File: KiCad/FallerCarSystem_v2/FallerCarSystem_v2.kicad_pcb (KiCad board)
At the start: 2 copper layers, 10 x 10 mm, 76 parts, among them J1 Conn_01x01_Male, J10 Conn_01x01_Male, J11 Conn_01x01_Male, J12 Conn_01x01_Male, J13 Conn_01x01_Male, J14 Conn_01x01_Male, J15 Conn_01x01_Male, J16 Conn_01x01_Male, J17 Conn_01x01_Male, J18 Conn_01x01_Male, J19 Conn_01x01_Male, J2 Conn_01x01_Male, J20 Conn_01x01_Male, J21 Conn_01x01_Male, J22 Conn_01x01_Male, J23 Conn_01x01_Male, J24 Conn_01x01_Male, J25 Conn_01x01_Male, J26 Conn_01x01_Male, J27 Conn_01x01_Male, J28 Conn_01x01_Male, J29 Conn_01x01_Male, J3 Conn_01x01_Male, J30 Conn_01x01_Male, J31 Conn_01x01_Male, J32 Conn_01x01_Male, J33 Conn_01x01_Male, J34 Conn_01x01_Male, J35 Conn_01x01_Male, J36 Conn_01x01_Male, J37 Conn_01x01_Male, J38 Conn_01x01_Male, J4 Conn_01x01_Male, J5 Conn_01x01_Male, J6 Conn_01x01_Male, J7 Conn_01x01_Male, J8 Conn_01x01_Male, J9 Conn_01x01_Male, U1 PIC16F15345-I_GZ, U2 MCP73871-2AA, U3 MCP1725-ADJE_MC_DFN-8

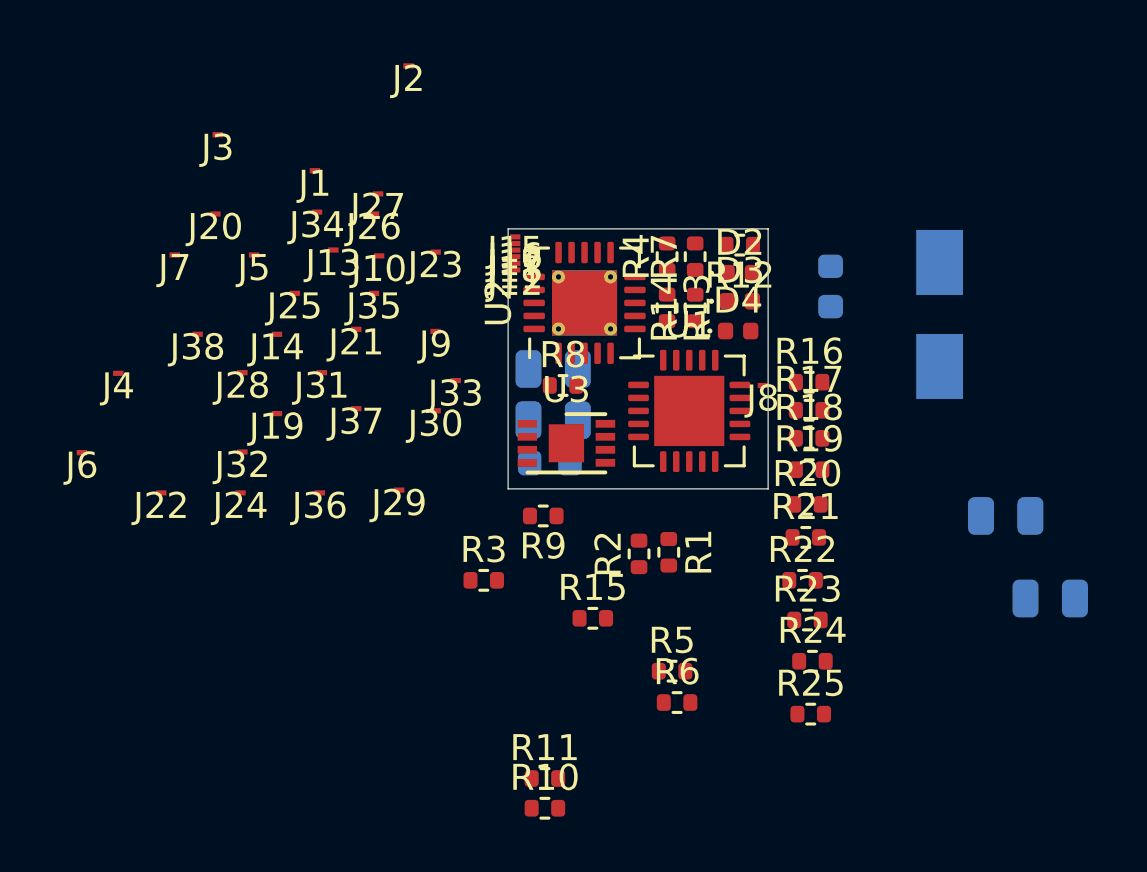
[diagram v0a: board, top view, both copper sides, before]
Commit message: FallerCarSystem_v2 drawing and PCB done. Generated Gerber files.
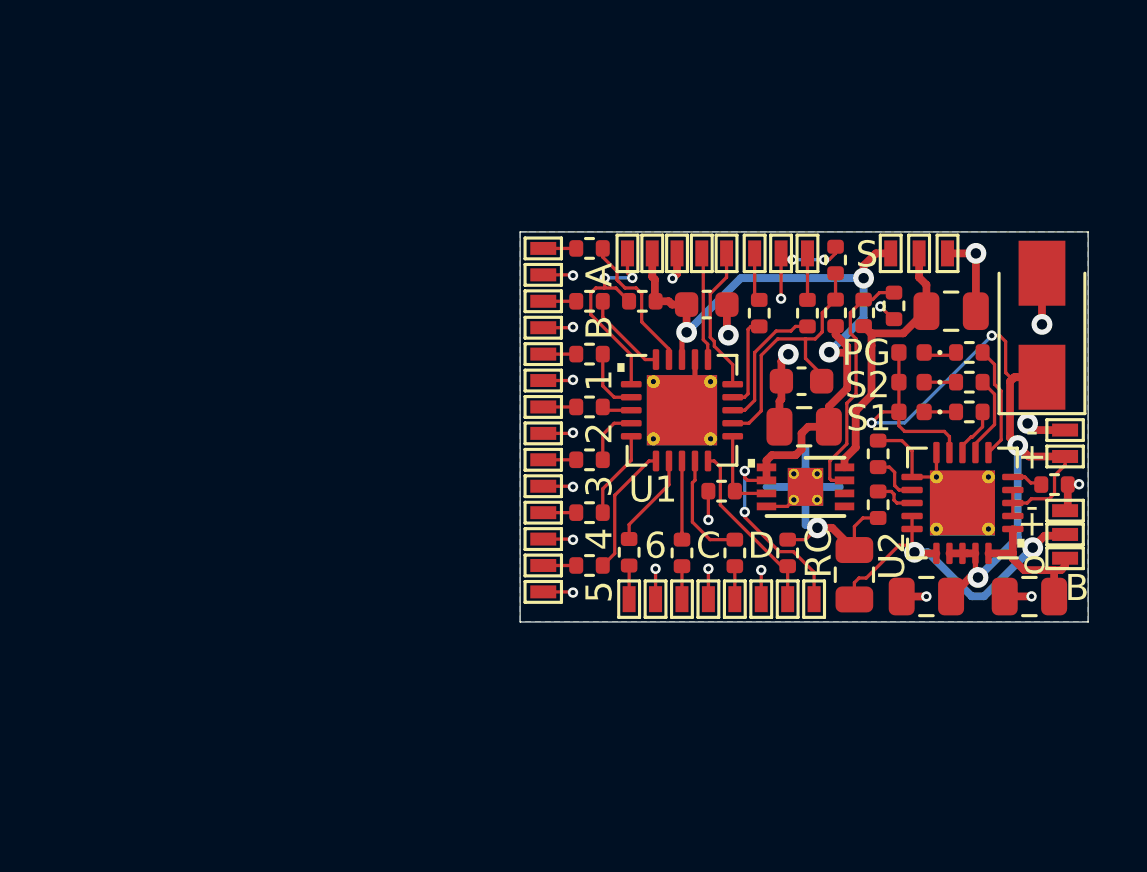
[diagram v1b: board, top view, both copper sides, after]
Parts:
- added C7: 4.7uF, Capacitor_SMD:C_0805_2012Metric, F.Cu at (160.0, 69.1)
- added REF**: ESD-Logo_6.6x6mm_SilkScreen, Symbol:ESD-Logo_6.6x6mm_SilkScreen, B.Cu at (156.7, 64.9)
- C1, C2, C3, C4, C5, C6, D1: moved to F.Cu
- J1, J10, J11, J12, J13, J14, J15, J16, J17, J18, J19, J2, J20, J21, J22, J23, J24, J25, J26, J27, J28, J29, J3, J30, J31, J32, J33, J34, J35, J36, J37, J38, J4, J5, J6, J7, J8, J9: footprint Connector:Finger -> TestPoint:TestPoint_Pad_0.5x1.0mm
- R10: value 4.7k -> 47k
- R11: value 10k2 -> 22k
- R3: value 1k -> 4k7
- R4: value 5k -> 18k
- R7: value 1k -> 220k
- U1: value PIC16F15345-I_GZ -> PIC16F15345-I_GZ-MCU_Microchip_PIC16; footprint Package_DFN_QFN:QFN-20-1EP_4x4mm_P0.5mm_EP2.7x2.7mm -> Package_DFN_QFN:QFN-20-1EP_4x4mm_P0.5mm_EP2.7x2.7mm_ThermalVias
- U3: value MCP1725-ADJE_MC_DFN-8 -> MCP1725-ADJE_MC_DFN-8-Regulator_Linear; footprint Package_DFN_QFN:DFN-8-1EP_3x2mm_P0.5mm_EP1.36x1.46mm -> Package_DFN_QFN:DFN-8-1EP_3x2mm_P0.5mm_EP1.36x1.46mm_ThermalVias
- moved J6 24.1 mm to (146.5, 55.9), turned to 90 degrees
- moved J11 24.0 mm to (161.4, 67.7), turned to 180 degrees
- moved J17 23.8 mm to (161.4, 66.8)
- moved J18 23.3 mm to (161.4, 65.8)
- moved J13 22.8 mm to (151.8, 69.2), turned to 90 degrees
- moved J15 22.8 mm to (161.4, 63.8), turned to 180 degrees
- moved R10 22.7 mm to (153.7, 58.2), turned to 270 degrees
- moved R11 22.6 mm to (154.8, 58.0), turned to 90 degrees
- moved J16 22.3 mm to (161.4, 62.7)
- moved J3 22.1 mm to (150.5, 55.9), turned to 90 degrees
- moved J38 22.1 mm to (147.7, 69.2), turned to 90 degrees
- moved J14 22.1 mm to (150.7, 69.2), turned to 90 degrees
- moved J10 21.9 mm to (156.9, 55.9), turned to 270 degrees
- moved J7 20.3 mm to (147.4, 55.9), turned to 270 degrees
- moved J4 20.1 mm to (144.6, 55.9), turned to 90 degrees
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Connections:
- net Net-(R12-Pad1) renamed /PG
- net Net-(R13-Pad1) renamed /STAT1
- net Net-(R14-Pad1) renamed /STAT2
- net VBATT renamed BATT
- R22 pad 2: (no net) -> LEDB
- R23 pad 2: LEDB -> LEDA
- R24 pad 2: LEDC -> LEDD
- R25 pad 2: LEDD -> LEDC
- U1 pad 10: LEDC -> RCS_IN
- U1 pad 12: PWM4 -> Vbatt
- U1 pad 13: Vbatt -> Net-(R5-Pad2)
- U1 pad 14: PWM3 -> Net-(R6-Pad2)
- U1 pad 19: LEDB -> LEDA
- U1 pad 20: (no net) -> LEDB
- U1 pad 21: (no net) -> GND
- U1 pad 3: RCS_IN -> PWM2
- U1 pad 4: PWM2 -> PWM3
- U1 pad 5: PWM5 -> PWM4
- U1 pad 6: PWM6 -> PWM5
- U1 pad 7: Net-(R6-Pad2) -> PWM6
- U1 pad 8: Net-(R5-Pad2) -> LEDC
- U3 pad 5: (no net) -> Net-(U3-Pad5)
- U3 pad 6: (no net) -> Net-(U3-Pad6)
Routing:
- net GND: track 0.00 -> 52.3 mm, vias 0 -> 25
- net +5V: track 0.00 -> 34.8 mm, vias 0 -> 4
- net +3V8: track 0.00 -> 34.7 mm, vias 0 -> 5
- net BATT: track 0.00 -> 13.0 mm, vias 0 -> 2
- net MOTOR+: track 0.00 -> 11.2 mm
- net Vbatt: track 0.00 -> 10.6 mm
- net Net-(R10-Pad1): track 0.00 -> 9.38 mm
- net Vpp: track 0.00 -> 8.39 mm, vias 0 -> 2
- net RCS_IN: track 0.00 -> 6.86 mm
- net SWONOFF_OUT: track 0.00 -> 5.84 mm
- net ICSPCLK: track 0.00 -> 5.65 mm
- net LEDA: track 0.00 -> 5.58 mm
- net Net-(R5-Pad2): track 0.00 -> 5.29 mm
- net PWM5: track 0.00 -> 5.02 mm
- net /PG: track 0.00 -> 4.35 mm
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- added copper zone on B.Cu, net GND
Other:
- board size 10 x 10 mm -> 21.8 x 15 mm
- net class Default: clearance 0.2 -> 0.127; trace_width 0.25 -> 0.2
- net class Power added: clearance 0.127, trace_width 0.3, via_dia 0.8, via_drill 0.4
- net class smallest added: clearance 0.127, trace_width 0.127, via_dia 0.4, via_drill 0.2
- rule trace_clearance: 0.2 -> 0.127
- rule trace_min: 0.2 -> 0.127
- rule via_min_drill: 0.3 -> 0.2
- board text added: "+"
- board text added: "-"
- board text added: "-MSW T-RCD-+V"
- board text added: "."
- board text added: "1"
- board text added: "2"
- board text added: "2023 0101"
- board text added: "3"
- board text added: "4"
- board text added: "5"
- board text added: "6"
- board text added: "A"
- board text added: "B"
- board text added: "BATT"
- board text added: "C"
- board text added: "D"
- board text added: "IN 5V DC"
- board text added: "JSIF FCAR"
- board text added: "PG"
- board text added: "RC"
- board text added: "S"
- board text added: "S1"
- board text added: "S2"
- board text added: "o"
